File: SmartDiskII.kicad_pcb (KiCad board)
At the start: 2 copper layers, 100 x 77.5 mm, 42 parts, among them J1 Apple II Expansion Slot, J2 DRV, U1 74LS174, U10 27C256, U11 74LS245, U12 74LS323, U13 74LS00, U14 74LS174, U2 NE556, U3 74LS05, U4 74LS132, U5 74LS259/9334, U6 74LS20, U7 74LS21, U8 2758/16/32 P6, U9 74LS30

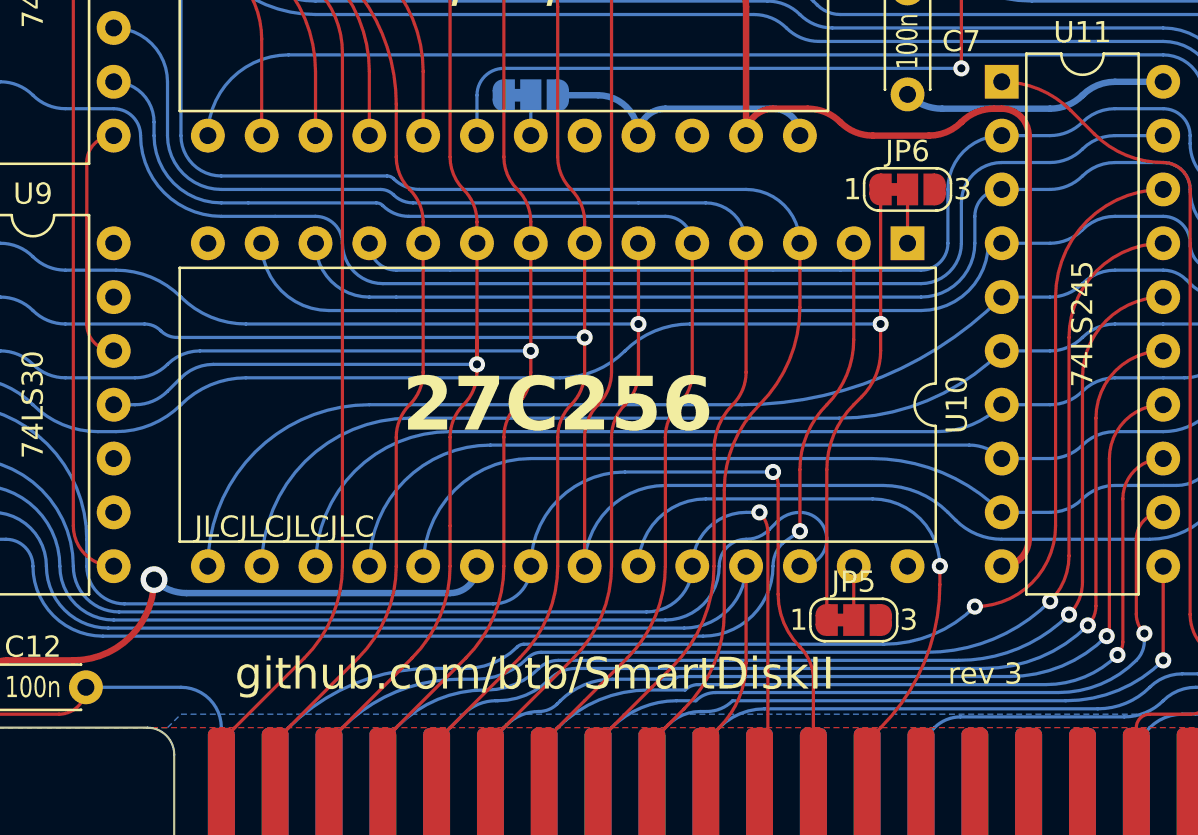
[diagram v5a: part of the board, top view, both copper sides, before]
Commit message: fix jumper, tweaks
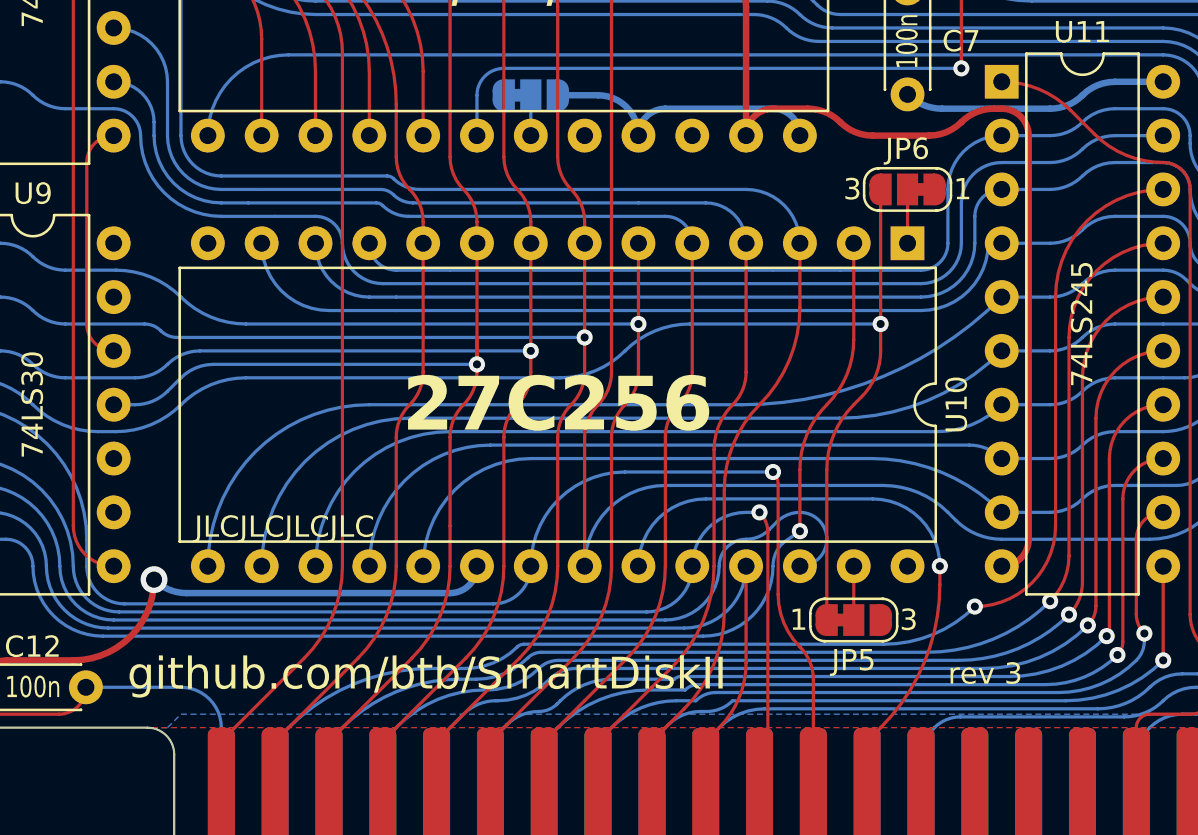
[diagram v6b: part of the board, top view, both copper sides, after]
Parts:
- turned JP6 to 180 degrees
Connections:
- JP6 pad 1: /LA14 -> +5V
- JP6 pad 3: +5V -> /LA14
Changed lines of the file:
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@@
   )
   (footprint "Jumper:SolderJumper-3_P1.3mm_Bridged12_RoundedPad1.0x1.5mm_NumberLabels" (layer "F.Cu")
-    (at 170.815 107.95)
+    (at 170.815 107.95 180)
     (descr "SMD Solder 3-pad Jumper, 1x1.5mm rounded Pads, 0.3mm gap, pads 1-2 bridged with 1 copper strip, labeled with numbers")
     (tags "net tie solder jumper bridged")
@@
     (attr exclude_from_pos_files)
     (net_tie_pad_groups "1, 2, 3")
-    (fp_text reference "JP6" (at 0 -1.8) (layer "F.SilkS")
+    (fp_text reference "JP6" (at 0 1.905) (layer "F.SilkS")
         (effects (font (size 1 1) (thickness 0.15)))
     )
@@
     (fp_line (start 2.3 1.25) (end 2.3 -1.25)
       (stroke (width 0.05) (type solid)) (layer "F.CrtYd"))
-    (pad "1" smd custom (at -1.3 0) (size 1 0.5) (layers "F.Cu" "F.Mask")
-      (net 100 "/LA14") (pinfunction "A") (pintype "passive") (zone_connect 2) (thermal_bridge_angle 45)
+    (pad "1" smd custom (at -1.3 0 180) (size 1 0.5) (layers "F.Cu" "F.Mask")
+      (net 4 "+5V") (pinfunction "A") (pintype "passive") (zone_connect 2) (thermal_bridge_angle 45)
       (options (clearance outline) (anchor rect))
       (primitives
@@
         (gr_circle (center 0 -0.25) (end 0.5 -0.25) (width 0) (fill yes))
       ))
-    (pad "2" smd rect (at 0 0) (size 1 1.5) (layers "F.Cu" "F.Mask")
+    (pad "2" smd rect (at 0 0 180) (size 1 1.5) (layers "F.Cu" "F.Mask")
       (net 124 "Net-(JP6-C)") (pinfunction "C") (pintype "passive"))
-    (pad "3" smd custom (at 1.3 0) (size 1 0.5) (layers "F.Cu" "F.Mask")
-      (net 4 "+5V") (pinfunction "B") (pintype "passive") (zone_connect 2) (thermal_bridge_angle 45)
+    (pad "3" smd custom (at 1.3 0 180) (size 1 0.5) (layers "F.Cu" "F.Mask")
+      (net 100 "/LA14") (pinfunction "B") (pintype "passive") (zone_connect 2) (thermal_bridge_angle 45)
       (options (clearance outline) (anchor rect))
       (primitives
@@
     (attr exclude_from_pos_files)
     (net_tie_pad_groups "1, 2, 3")
-    (fp_text reference "JP5" (at 0 -1.8) (layer "F.SilkS")
+    (fp_text reference "JP5" (at 0 1.905) (layer "F.SilkS")
         (effects (font (size 1 1) (thickness 0.15)))
     )
@@
     (effects (font (size 1 1) (thickness 0.15)) (justify left))
   )
-  (gr_text "github.com/btb/SmartDiskII" (at 139.065 130.81) (layer "F.SilkS")
+  (gr_text "github.com/btb/SmartDiskII" (at 133.985 130.81) (layer "F.SilkS")
     (effects (font (size 1.5 1.5) (thickness 0.3)) (justify left))
   )

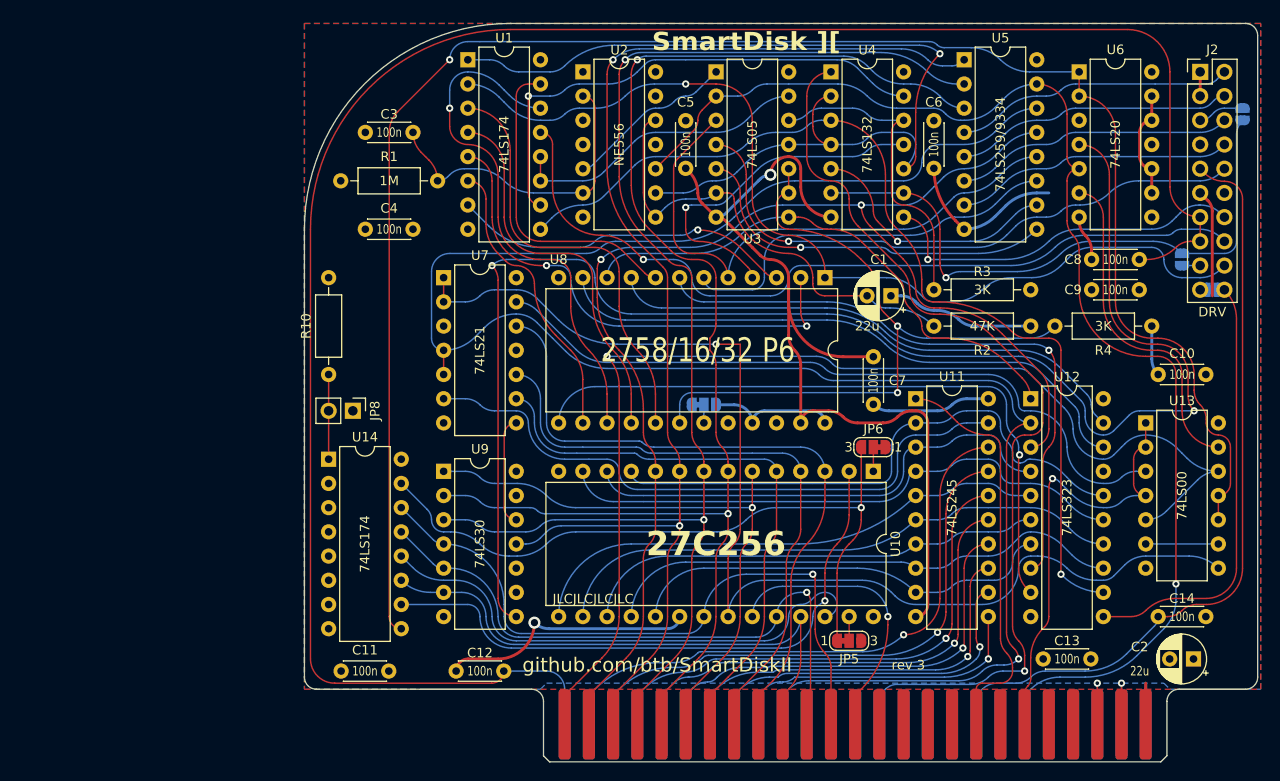
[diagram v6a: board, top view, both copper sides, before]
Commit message: Working circuit for multi-rom
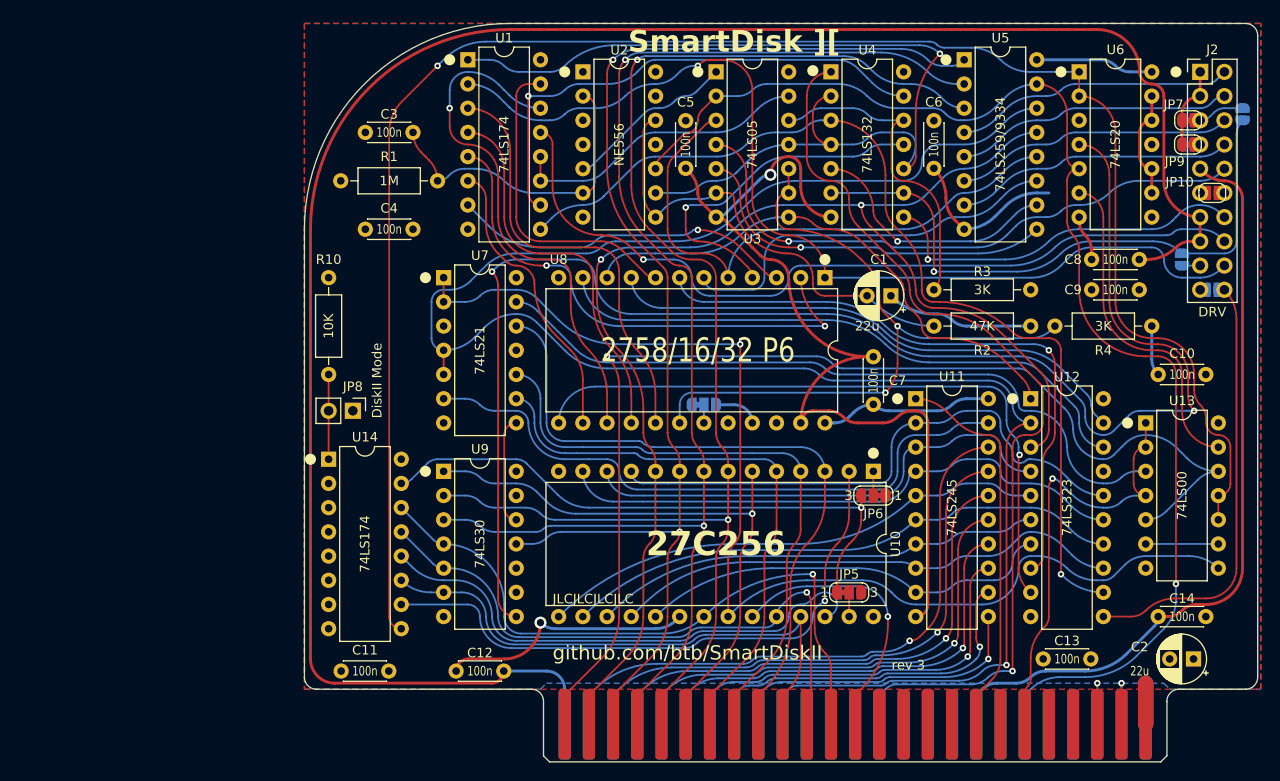
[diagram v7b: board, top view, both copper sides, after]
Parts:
- added JP10: ~, Jumper:SolderJumper-2_P1.3mm_Open_RoundedPad1.0x1.5mm, F.Cu at (206.4, 81.3)
- added JP7: ~, Jumper:SolderJumper-2_P1.3mm_Bridged_RoundedPad1.0x1.5mm, F.Cu at (203.8, 73.7)
- added JP9: ~, Jumper:SolderJumper-2_P1.3mm_Bridged_RoundedPad1.0x1.5mm, F.Cu at (203.8, 76.2)
- JP8: value ~ -> DiskII Mode
- moved JP5 5.08 mm to (168.3, 123.2)
- moved JP6 5.08 mm to (170.8, 113.0)
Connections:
- net /LA12 renamed Net-(U10-A12)
- net /LA13 renamed Net-(U10-A13)
- net /LA14 renamed Net-(JP5-A)
- J2 pad 7: unconnected-(J2-Pin_7-Pad7) -> Net-(J2-Pin_7)
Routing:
- net Net-(JP5-A): track 73.7 -> 61.8 mm
- net /~{DEVSEL}: track 203.9 -> 200.5 mm
- net Net-(U1-Q1): track 52.0 -> 54.5 mm
- net /R/W: track 43.0 -> 40.6 mm
- net +5V: track 62.8 -> 60.6 mm
- net /WR DATA: track 100.8 -> 103.0 mm
- net /R3: track 55.5 -> 53.4 mm
- net /R4: track 60.6 -> 58.6 mm
- net /A1: track 131.6 -> 129.8 mm
- net /A10: track 69.8 -> 68.1 mm
- net /R5: track 48.8 -> 47.1 mm
- net /Q3: track 98.0 -> 96.4 mm
- net +12V: track 208.5 -> 207.0 mm
- net /R7: track 45.0 -> 43.6 mm
- net /R6: track 55.0 -> 53.6 mm
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
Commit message: invert /SEL for auto detect of 5.25 floppy
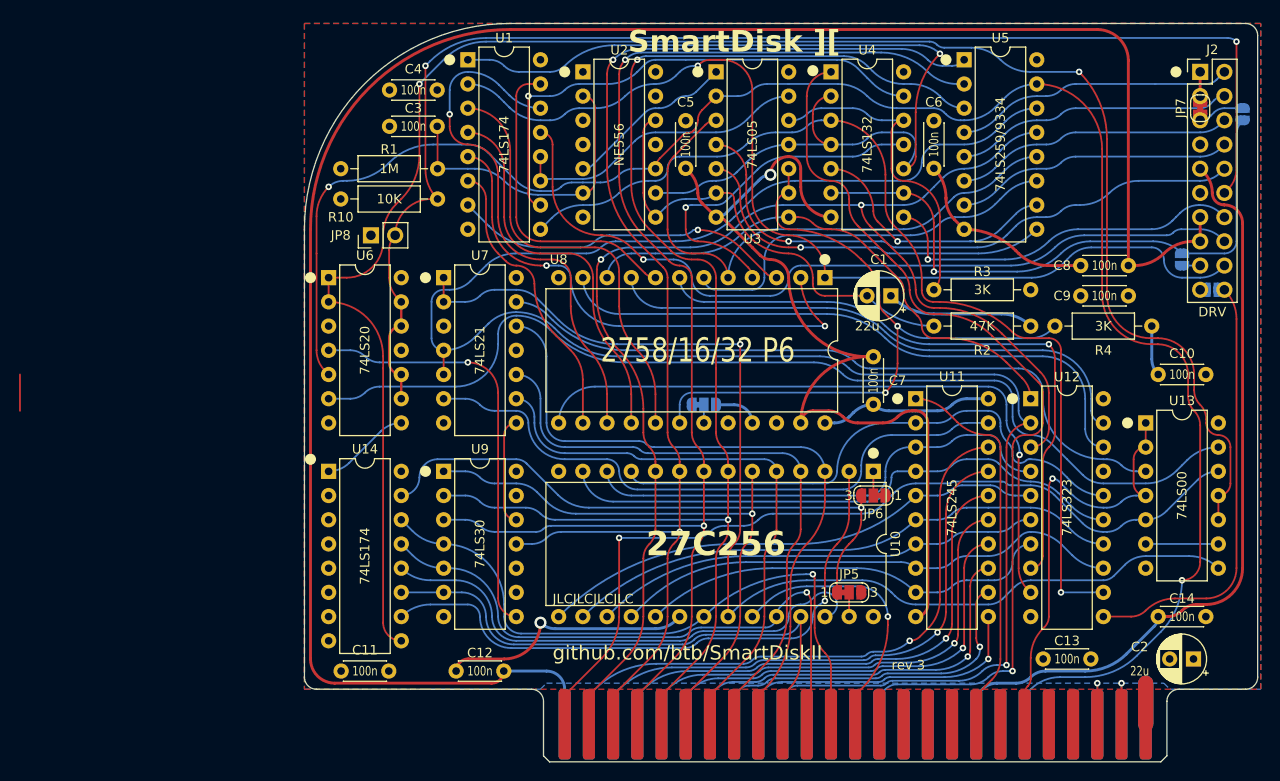
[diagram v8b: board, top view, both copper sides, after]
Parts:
- removed JP10: ~, Jumper:SolderJumper-2_P1.3mm_Open_RoundedPad1.0x1.5mm
- removed JP9: ~, Jumper:SolderJumper-2_P1.3mm_Bridged_RoundedPad1.0x1.5mm
- moved U6 81.6 mm to (113.7, 90.2)
- moved R10 21.7 mm to (125.1, 81.9), turned to 180 degrees
- moved JP8 18.5 mm to (118.1, 85.7), turned to 90 degrees
- moved C4 14.8 mm to (120.1, 70.5)
- moved C3 2.62 mm to (125.1, 74.3)
- moved JP7 1.80 mm to (205.1, 72.4), turned to -90 degrees
- moved C8 1.31 mm to (197.6, 88.9)
- moved C9 1.31 mm to (192.6, 92.1)
- moved R1 1.27 mm to (114.9, 78.7)
- moved U14 1.27 mm to (113.7, 110.5)
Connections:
- J2 pad 7: Net-(J2-Pin_7) -> /~{EN3.5}
- JP8 pad 1: GND -> +5V
- JP8 pad 2: Net-(JP8-B) -> /SEL
- R10 pad 1: Net-(JP8-B) -> /SEL
- R10 pad 2: +5V -> GND
- U14 pad 1: Net-(JP8-B) -> Net-(U14-~{Mr})
- U6 pad 10: GND -> /SEL
- U6 pad 12: GND -> /SEL
- U6 pad 13: GND -> /SEL
- U6 pad 8: unconnected-(U6-Pad8) -> Net-(U14-~{Mr})
- U6 pad 9: GND -> /SEL
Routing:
- net /SEL: track 0.00 -> 145.9 mm, vias 0 -> 2
- net /~{HISTROBE}: track 155.0 -> 44.3 mm, vias 2 -> 1
- net /CLRCOMMON: track 34.7 -> 106.7 mm
- net /~{RES}: track 133.1 -> 192.0 mm, vias 1 -> 2
- net /~{IOSEL}: track 121.6 -> 90.0 mm
- net GND: track 169.8 -> 150.6 mm
- net +5V: track 60.6 -> 48.0 mm
- net Net-(U14-~{Mr}): track 0.00 -> 9.43 mm
- net Net-(JP8-B): track 8.89 -> 0.00 mm
- net /ENCOMMON: track 186.5 -> 194.3 mm, vias 1 -> 2
- net /~{ENROM}: track 122.3 -> 119.8 mm
- net +12V: track 207.0 -> 209.4 mm
- net Net-(U2A-THR): track 34.2 -> 31.9 mm
- net Net-(U12-DS7): track 62.6 -> 64.3 mm
- net Net-(U1-Cp): track 101.4 -> 103.0 mm
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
